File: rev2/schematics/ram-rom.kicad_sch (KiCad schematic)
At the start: 7 parts, among them U10 28C256, U11 28C256, U12 MT16D832

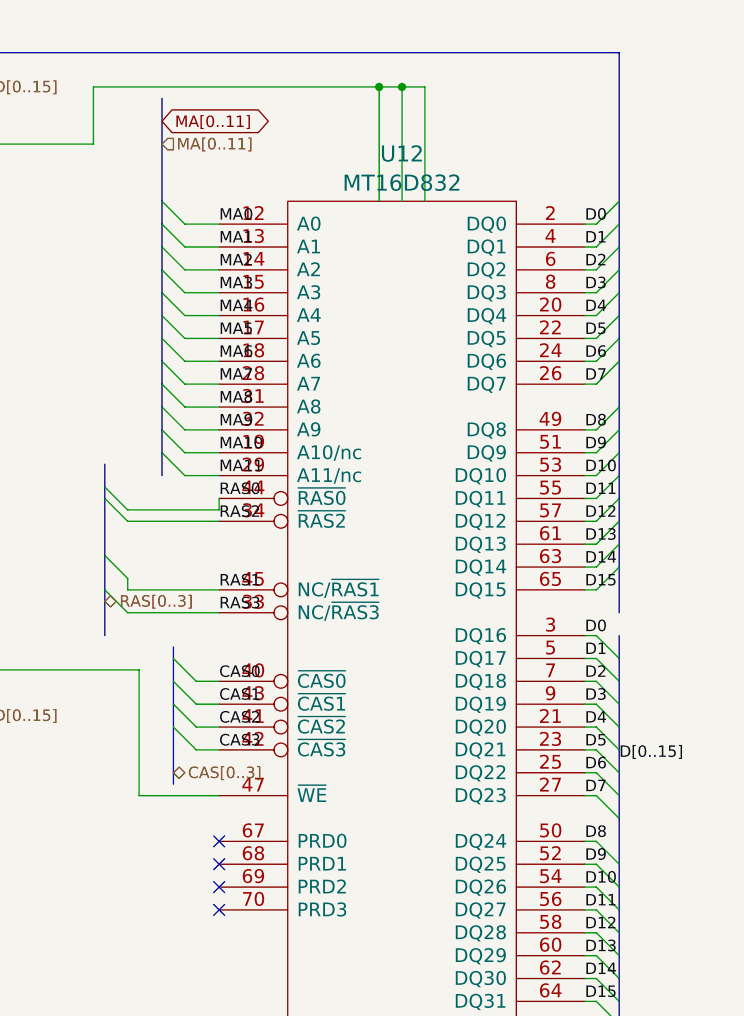
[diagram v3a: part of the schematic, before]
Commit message: Added SIMM footprint and Raven logo. Did initial PCB component placement and routing using autorouter. Still needs to be checked before ordering PCBs to verify on an actual hardware.
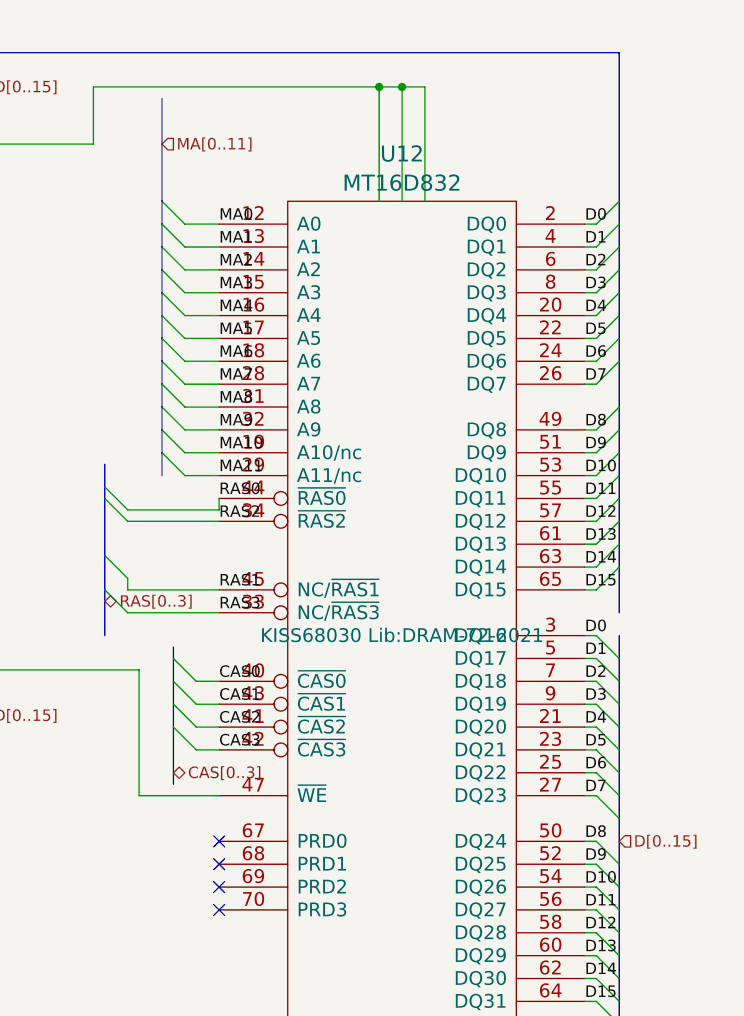
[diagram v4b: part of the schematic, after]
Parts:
- U12: footprint (none) -> KISS68030 Lib:DRAM-72-2021; symbol kiss030 lib:MT16D832 -> KISS68030 Rescue:MT16D832
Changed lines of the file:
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@@
     (effects (font (size 1.27 1.27)) (justify left bottom))
   )
-  (label "D13" (at 250.19 123.19 0)
-    (effects (font (size 1.27 1.27)) (justify left bottom))
-  )
-  (label "D7" (at 250.19 105.41 0)
+  (label "D13" (at 250.19 123.19 0) (fields_autoplaced)
+    (effects (font (size 1.27 1.27)) (justify left bottom))
+  )
+  (label "D7" (at 250.19 105.41 0) (fields_autoplaced)
     (effects (font (size 1.27 1.27)) (justify left bottom))
   )
@@
     (effects (font (size 1.27 1.27)) (justify left bottom))
   )
-  (label "D11" (at 250.19 118.11 0)
+  (label "D11" (at 250.19 118.11 0) (fields_autoplaced)
     (effects (font (size 1.27 1.27)) (justify left bottom))
   )
@@
     (effects (font (size 1.27 1.27)) (justify left bottom))
   )
-  (label "D[0..15]" (at 254 101.6 0) (fields_autoplaced)
-    (effects (font (size 1.27 1.27)) (justify left bottom))
-  )
-  (label "D14" (at 250.19 125.73 0)
-    (effects (font (size 1.27 1.27)) (justify left bottom))
-  )
-  (label "D15" (at 250.19 128.27 0)
+  (label "D14" (at 250.19 125.73 0) (fields_autoplaced)
+    (effects (font (size 1.27 1.27)) (justify left bottom))
+  )
+  (label "D15" (at 250.19 128.27 0) (fields_autoplaced)
     (effects (font (size 1.27 1.27)) (justify left bottom))
   )
@@
     (effects (font (size 1.27 1.27)) (justify left bottom))
   )
-  (label "D1" (at 250.19 90.17 0)
-    (effects (font (size 1.27 1.27)) (justify left bottom))
-  )
-  (label "D6" (at 250.19 102.87 0)
+  (label "D1" (at 250.19 90.17 0) (fields_autoplaced)
+    (effects (font (size 1.27 1.27)) (justify left bottom))
+  )
+  (label "D6" (at 250.19 102.87 0) (fields_autoplaced)
     (effects (font (size 1.27 1.27)) (justify left bottom))
   )
@@
     (effects (font (size 1.27 1.27)) (justify left bottom))
   )
-  (label "D12" (at 250.19 120.65 0)
+  (label "D12" (at 250.19 120.65 0) (fields_autoplaced)
     (effects (font (size 1.27 1.27)) (justify left bottom))
   )
@@
     (effects (font (size 1.27 1.27)) (justify left bottom))
   )
-  (label "D2" (at 250.19 92.71 0)
+  (label "D2" (at 250.19 92.71 0) (fields_autoplaced)
     (effects (font (size 1.27 1.27)) (justify left bottom))
   )
@@
     (effects (font (size 1.27 1.27)) (justify left bottom))
   )
-  (label "D10" (at 250.19 115.57 0)
+  (label "D10" (at 250.19 115.57 0) (fields_autoplaced)
     (effects (font (size 1.27 1.27)) (justify left bottom))
   )
@@
     (effects (font (size 1.27 1.27)) (justify left bottom))
   )
-  (label "D4" (at 250.19 97.79 0)
+  (label "D4" (at 250.19 97.79 0) (fields_autoplaced)
     (effects (font (size 1.27 1.27)) (justify left bottom))
   )
@@
     (effects (font (size 1.27 1.27)) (justify left bottom))
   )
-  (label "D8" (at 250.19 110.49 0)
+  (label "D8" (at 250.19 110.49 0) (fields_autoplaced)
     (effects (font (size 1.27 1.27)) (justify left bottom))
   )
@@
     (effects (font (size 1.27 1.27)) (justify left bottom))
   )
-  (label "D3" (at 250.19 95.25 0)
+  (label "D3" (at 250.19 95.25 0) (fields_autoplaced)
     (effects (font (size 1.27 1.27)) (justify left bottom))
   )
@@
     (effects (font (size 1.27 1.27)) (justify left bottom))
   )
-  (label "D5" (at 250.19 100.33 0)
+  (label "D5" (at 250.19 100.33 0) (fields_autoplaced)
     (effects (font (size 1.27 1.27)) (justify left bottom))
   )
@@
     (effects (font (size 1.27 1.27)) (justify left bottom))
   )
-  (label "D9" (at 250.19 113.03 0)
+  (label "D9" (at 250.19 113.03 0) (fields_autoplaced)
     (effects (font (size 1.27 1.27)) (justify left bottom))
   )
@@
     (effects (font (size 1.27 1.27)) (justify left bottom))
   )
-  (label "D0" (at 250.19 87.63 0)
+  (label "D0" (at 250.19 87.63 0) (fields_autoplaced)
     (effects (font (size 1.27 1.27)) (justify left bottom))
   )
@@
   (label "A2" (at 151.13 40.64 0) (fields_autoplaced)
     (effects (font (size 1.27 1.27)) (justify left bottom))
-  )
-  (global_label "MA[0..11]" (shape bidirectional) (at 203.2 30.48 0) (fields_autoplaced)
-    (effects (font (size 1.27 1.27)) (justify left))
-    (property "Intersheetrefs" "${INTERSHEET_REFS}" (at 215.555 30.48 0)
-      (effects (font (size 1.27 1.27)) (justify left) hide)
-    )
   )
   (hierarchical_label "~{ROM_UCE}" (shape input) (at 144.78 83.82 180) (fields_autoplaced)
@@
   )
   (hierarchical_label "MA[0..11]" (shape input) (at 203.2 33.02 0) (fields_autoplaced)
+    (effects (font (size 1.27 1.27)) (justify left))
+  )
+  (hierarchical_label "D[0..15]" (shape input) (at 254 110.49 0) (fields_autoplaced)
     (effects (font (size 1.27 1.27)) (justify left))
   )
@@
     )
   )
-  (symbol (lib_id "kiss030 lib:MT16D832") (at 229.87 87.63 0) (unit 1)
+  (symbol (lib_id "KISS68030 Rescue:MT16D832") (at 229.87 87.63 0) (unit 1)
     (in_bom yes) (on_board yes) (dnp no) (fields_autoplaced)
     (property "Reference" "U12" (at 229.87 34.1266 0)
@@
       (effects (font (size 1.778 1.778)))
     )
-    (property "Footprint" "" (at 229.87 87.63 0)
+    (property "Footprint" "KISS68030 Lib:DRAM-72-2021" (at 229.87 87.63 0)
       (effects (font (size 1.524 1.524)))
     )
